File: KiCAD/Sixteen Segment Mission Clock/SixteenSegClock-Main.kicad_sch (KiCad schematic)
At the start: 45 parts, among them J101 Input, J102 Output, U101 AZ1117-5.0, U102 AZ1117-5.0

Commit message: Fixed regulator math, added to sixteen segment display
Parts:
- removed U102: AZ1117-5.0, Package_TO_SOT_SMD:SOT-223-3_TabPin2, symbol Regulator_Linear:AZ1117-5.0
- added U2: L78S05CV, Package_TO_SOT_THT:TO-220-3_Horizontal_TabDown, symbol Regulator_Linear:L7805
- renumbered C101 to C1, C110 to C10, C111 to C11, C102 to C2, C103 to C3, C104 to C4, C105 to C5, C106 to C6, C107 to C7, C108 to C8, C109 to C9, D101 to D1, D105 to D10, D106 to D11, D121 to D12, D122 to D13, D107 to D14, D119 to D15, D120 to D16, D109 to D17, D117 to D18, D118 to D19, D127 to D2, D108 to D20, D110 to D21, D114 to D22, D116 to D23, D111 to D24, D112 to D25, D113 to D26, D115 to D27, D103 to D3, D125 to D4, D126 to D5, D104 to D6, D102 to D7, D123 to D8, D124 to D9, H101 to H1, H102 to H2, J101 to J1, J102 to J2, R101 to R1, U101 to U1
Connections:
- net GND: now also U2.2 (GND)
- net V5_0: now also D11.2 (VCC), D13.2 (VCC), D16.2 (VCC), D19.2 (VCC), D21.2 (VCC), D23.2 (VCC), D25.2 (VCC), D5.2 (VCC), D7.2 (VCC), D9.2 (VCC), U2.3 (OUT)
- net VIN_12V: now also U2.1 (IN)
- net at D1.5 (GND), D11.5 (GND), D13.5 (GND)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: now also D10.5 (GND), D12.5 (GND), D15.5 (GND), D18.5 (GND), D20.5 (GND), D22.5 (GND), D24.5 (GND), D4.5 (GND), D6.5 (GND), D8.5 (GND)
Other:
- note added: "Each LED: 20mA + 20mA + 20mA = 60mA (R) (G) (B) 1*7 + 2*10 = 27 LEDs 27*60mA = 1,620mA"
- note added: "L78S05CV Max Input Voltage: 35V Max Output Current: 2,000mA"
- note removed: "Each LED: 20mA 1*7 + 2*10 = 27 27*20mA = 540mA"

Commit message: Added decoupling caps
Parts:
- added C12, C13, C14, C15, C16, C17, C18, C19, C20, C21, C22, C23, C24, C25, C26, C27: 1uF, Capacitor_SMD:C_0603_1608Metric_Pad1.08x0.95mm_HandSolder, symbol Device:C_Small
- added H2, H4: M4, MountingHole:MountingHole_4.3mm_M4_DIN965_Pad, symbol Mechanical:MountingHole_Pad
- renumbered H2 to H3
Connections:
- net GND: now also C12.2, C13.2, C14.2, C15.2, C16.2, C17.2, C18.2, C19.2, C20.2, C21.2, C22.2, C23.2, C24.2, C25.2, C26.2, C27.2
- net V5_0: now also C12.1, C13.1, C14.1, C15.1, C16.1, C17.1, C18.1, C19.1, C20.1, C21.1, C22.1, C23.1, C24.1, C25.1, C26.1, C27.1
- net at D1.5 (GND), D10.5 (GND), D11.5 (GND)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: now also H2.1, H4.1
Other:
- moved on the sheet: C10, C11

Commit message: Initial routings
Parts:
- removed C1, C2, C3, C5, C6, C8, C9: 1uF, Capacitor_SMD:C_0603_1608Metric_Pad1.08x0.95mm_HandSolder, symbol Device:C_Small
- removed C4, C7: 10uF, Capacitor_SMD:C_0603_1608Metric_Pad1.08x0.95mm_HandSolder, symbol Device:C_Polarized_US
- removed U1: AZ1117-5.0, Package_TO_SOT_SMD:SOT-223-3_TabPin2, symbol Regulator_Linear:AZ1117-5.0
- added C19: 1uF, Capacitor_SMD:C_0603_1608Metric_Pad1.08x0.95mm_HandSolder, symbol Device:C_Small
- renumbered C10 to C1, C19 to C10, C20 to C11, C21 to C12, C22 to C13, C23 to C14, C24 to C15, C25 to C16, C26 to C17, C27 to C18, C11 to C2, C12 to C3, C13 to C4, C14 to C5, C15 to C6, C16 to C7, C17 to C8, C18 to C9, U2 to U1
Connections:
- net GND: now also D1.5 (GND), D10.5 (GND), D11.5 (GND), D12.5 (GND), D13.5 (GND), D14.5 (GND), D15.5 (GND), D16.5 (GND), D17.5 (GND), D18.5 (GND), D19.5 (GND), D2.5 (GND), D20.5 (GND), D21.5 (GND), D22.5 (GND), D23.5 (GND), D24.5 (GND), D25.5 (GND), D26.5 (GND), D27.5 (GND), D3.5 (GND), D4.5 (GND), D5.5 (GND), D6.5 (GND), D7.5 (GND), D8.5 (GND), D9.5 (GND), H1.1, H2.1, H3.1, H4.1, J1.3 (Pin_3), J2.1 (Pin_1), C19.2
- net V5_0: now also C19.1
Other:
- note removed: "AZ1117 Max Input Voltage: 18V Max Output Current: 1,350mA"
- note removed: "Each LED: 20mA + 20mA + 20mA = 60mA 7*3 = 21 LEDs 21*60mA = 1,260mA"

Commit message: Routed all components
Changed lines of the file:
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@@
   )
   (text "L78S05CV\nMax Input Voltage: 35V\nMax Output Current: 2,000mA"
-    (at -112.395 73.025 0)
+    (at 173.355 248.285 0)
     (effects (font (size 5.08 5.08)) (justify left bottom))
   )

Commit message: Rounded corners
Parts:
- removed U1: L78S05CV, Package_TO_SOT_THT:TO-220-3_Horizontal_TabDown, symbol Regulator_Linear:L7805
- added U1: AZ1117-5.0, Package_TO_SOT_SMD:SOT-223-3_TabPin2, symbol Regulator_Linear:AZ1117-5.0
- C2: value 10uF -> 22uF
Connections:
- net GND: now also U1.1 (GND)
- net V5_0: now also U1.2 (VO)
- net VIN_12V: now also U1.3 (VI)
- net A1-A2 renamed A1-A2L
- net A2-B renamed A2-BL
- net B-C renamed B-CL
- net C-D2 renamed C-D2L
- net D1-E renamed D1-EL
- net D2-D1 renamed D2-D1L
- net E-F renamed E-FL
- net F-G1 renamed F-G1L
- net G1-G2 renamed G1-G2L
- net G2-H renamed G2-HL
- net H-I renamed H-IR
- net I-J renamed I-JR
- net J-K renamed J-KR
- net K-L renamed K-LR
- net L-M renamed L-MR
- net M-DP renamed M-DPR
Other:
- note added: "AZ1117-5.0"
- note added: "Each LED: 16mA + 16mA + 16mA = 48mA (R) (G) (B) 1*7 + 2*10 = 27 LEDs 27*48mA = 1,296mA"
- note added: "Max Input Voltage: 18V Configured Output Voltage: 5V Max Output Current: 1,350mA 5V * 1,350mA = 6.75W Consumed 6.75W/12V = 563mA Input"
- note removed: "Each LED: 20mA + 20mA + 20mA = 60mA (R) (G) (B) 1*7 + 2*10 = 27 LEDs 27*60mA = 1,620mA"
- note removed: "L78S05CV Max Input Voltage: 35V Max Output Current: 2,000mA"
- moved on the sheet: D10, D11, D12, D13, D14, D15, D16, D17, D18, D19, D20, D21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

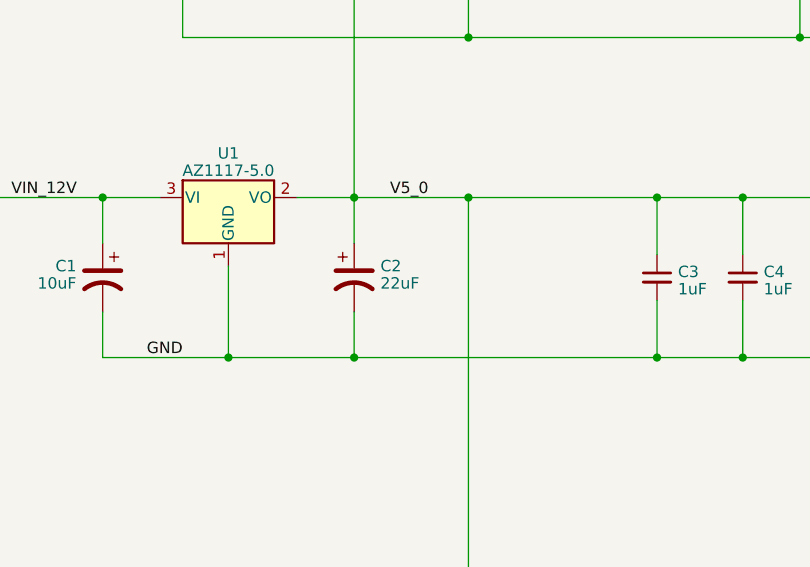
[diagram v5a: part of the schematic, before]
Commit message: Renamed 22uF to 10uF
Due to component availability
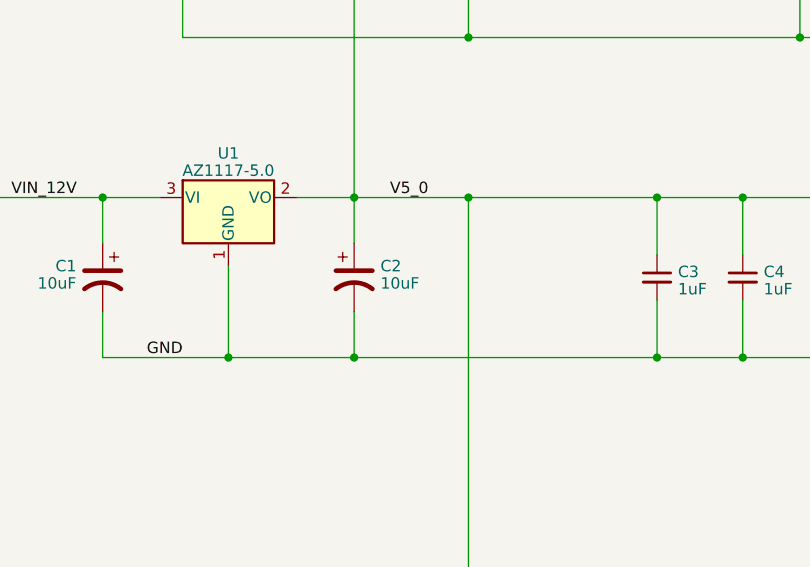
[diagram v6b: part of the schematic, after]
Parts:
- C2: value 22uF -> 10uF
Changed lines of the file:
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@@
       (effects (font (size 1.27 1.27)) (justify left))
     )
-    (property "Value" "22uF" (at 59.436 99.0673 0)
+    (property "Value" "10uF" (at 59.436 99.0673 0)
       (effects (font (size 1.27 1.27)) (justify left))
     )
